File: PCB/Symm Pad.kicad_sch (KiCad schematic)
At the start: 21 parts, among them J1 0.91{dblquote}_OLED_Display, SW1 SW_Push, SW2 SW_Push, SW3 SW_Push, SW4 SW_Push, SW5 SW_Push, SW6 SW_Push, SW7 RotaryEncoder_Switch, U1 XIAO-RP2040-DIP

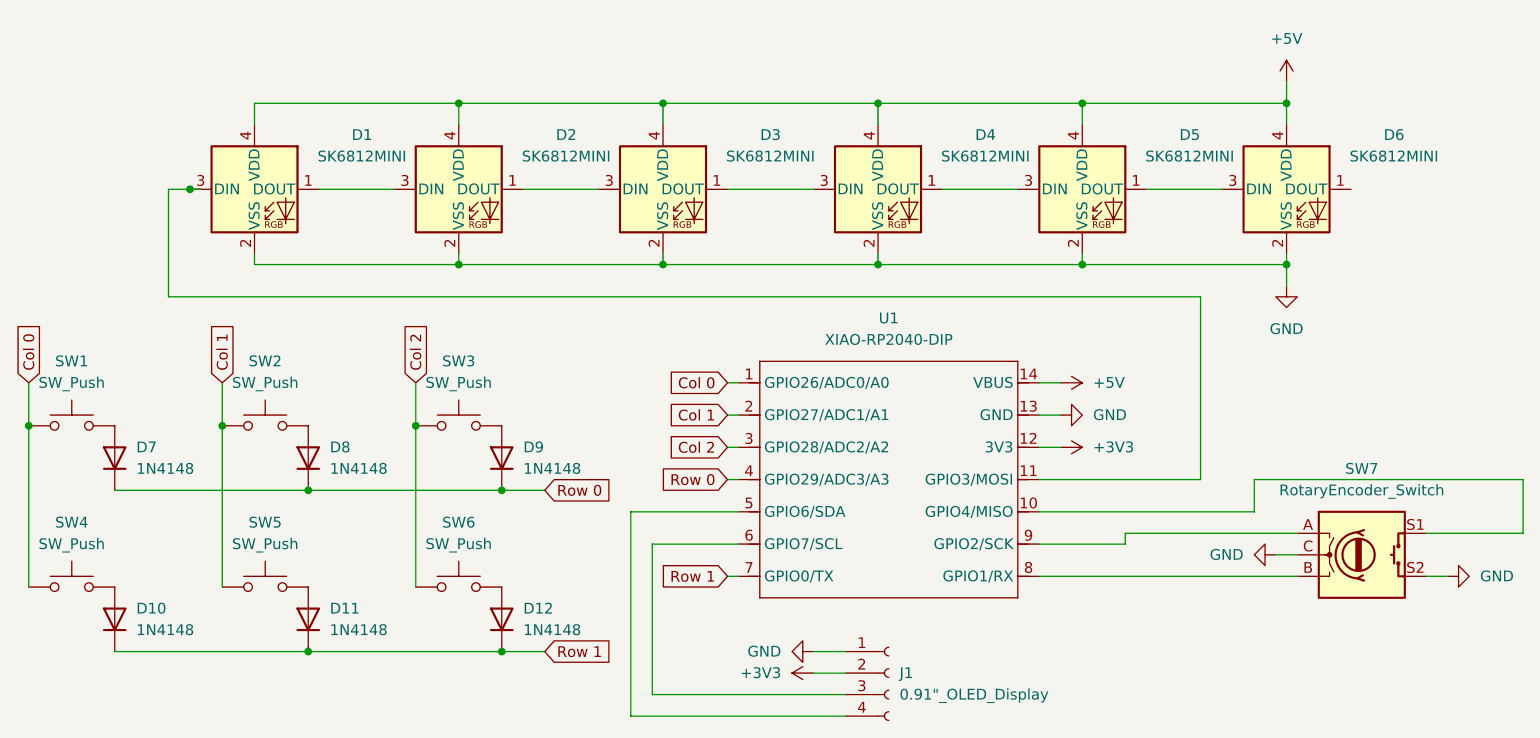
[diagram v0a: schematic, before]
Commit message: Correct footprint of neopixels
Earlier the SK6812 MINI footprint was being used which wasn't correct. Now changed to SK6812 MINI-E footprints.
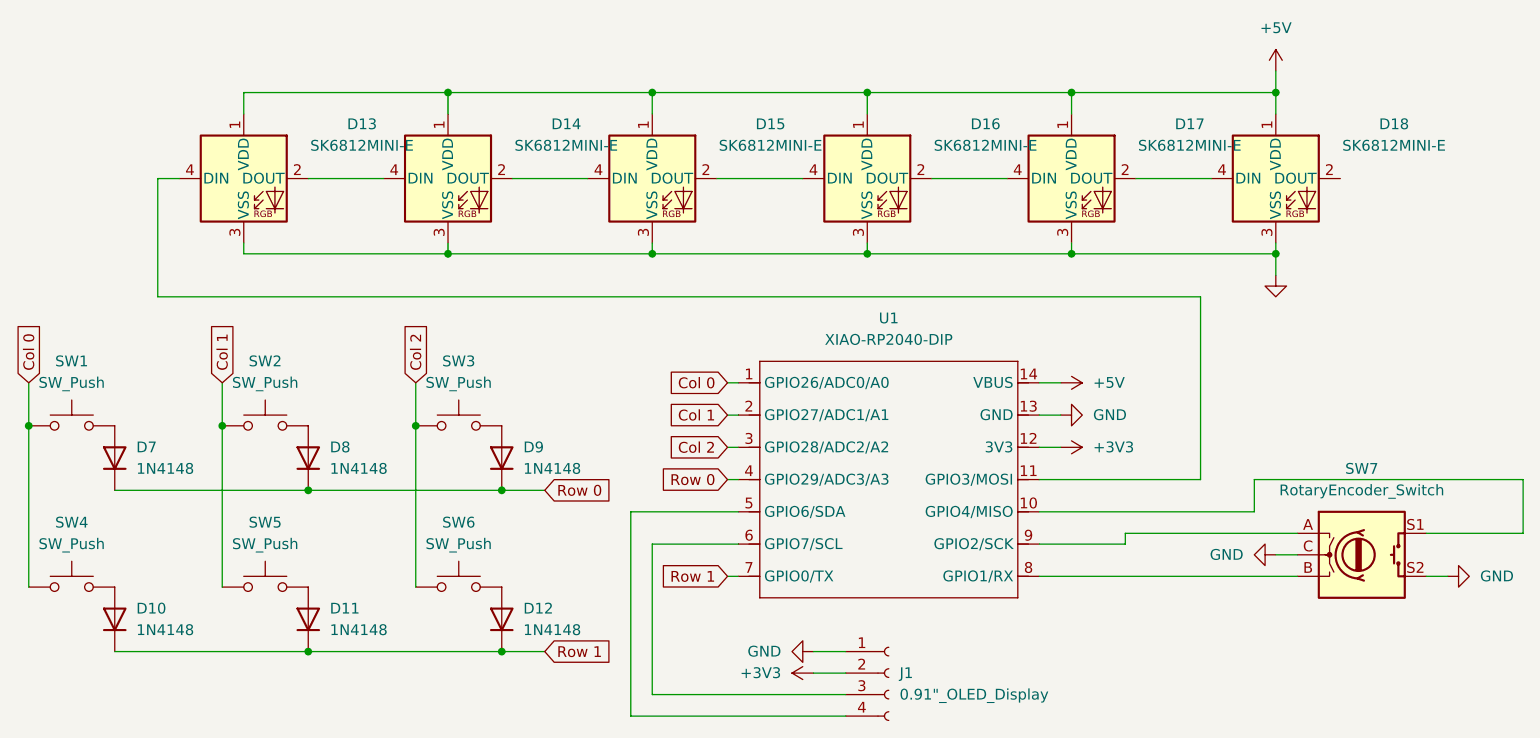
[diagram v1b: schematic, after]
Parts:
- removed D1, D2, D3, D4, D5, D6: SK6812MINI, LED_SMD:LED_SK6812MINI_PLCC4_3.5x3.5mm_P1.75mm, symbol LED:SK6812MINI
- added D13, D14, D15, D16, D17, D18: SK6812MINI-E, kicad-keyboard-parts:MX_SK6812MINI-E, symbol kicad-keyboard-parts:SK6812MINI-E
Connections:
- net +5V: now also D13.1 (VDD), D14.1 (VDD), D15.1 (VDD), D16.1 (VDD), D17.1 (VDD), D18.1 (VDD)
- net GND: now also D13.3 (VSS), D14.3 (VSS), D15.3 (VSS), D16.3 (VSS), D17.3 (VSS), D18.3 (VSS)
- net at U1.11 (GPIO3/MOSI): now also D13.4 (DIN)
- new net: D13.2 (DOUT), D14.4 (DIN)
- new net: D16.2 (DOUT), D17.4 (DIN)
- new net: D15.2 (DOUT), D16.4 (DIN)
- new net: D14.2 (DOUT), D15.4 (DIN)
- new net: D17.2 (DOUT), D18.4 (DIN)
